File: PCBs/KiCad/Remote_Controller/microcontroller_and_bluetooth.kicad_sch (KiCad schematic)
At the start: 19 parts

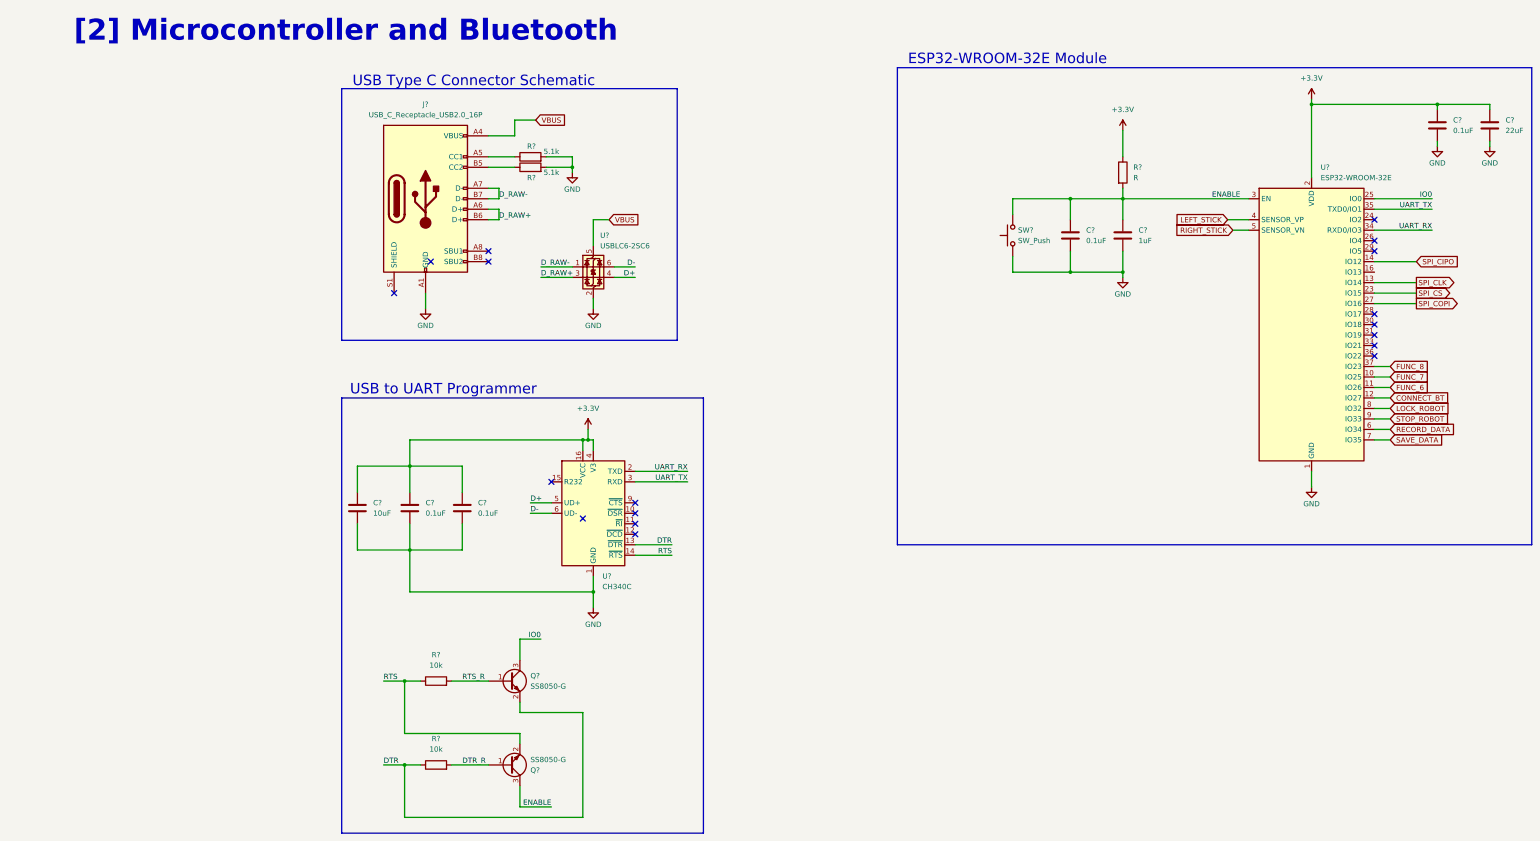
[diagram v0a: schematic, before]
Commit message: Add Power on indicator light, made small corrections
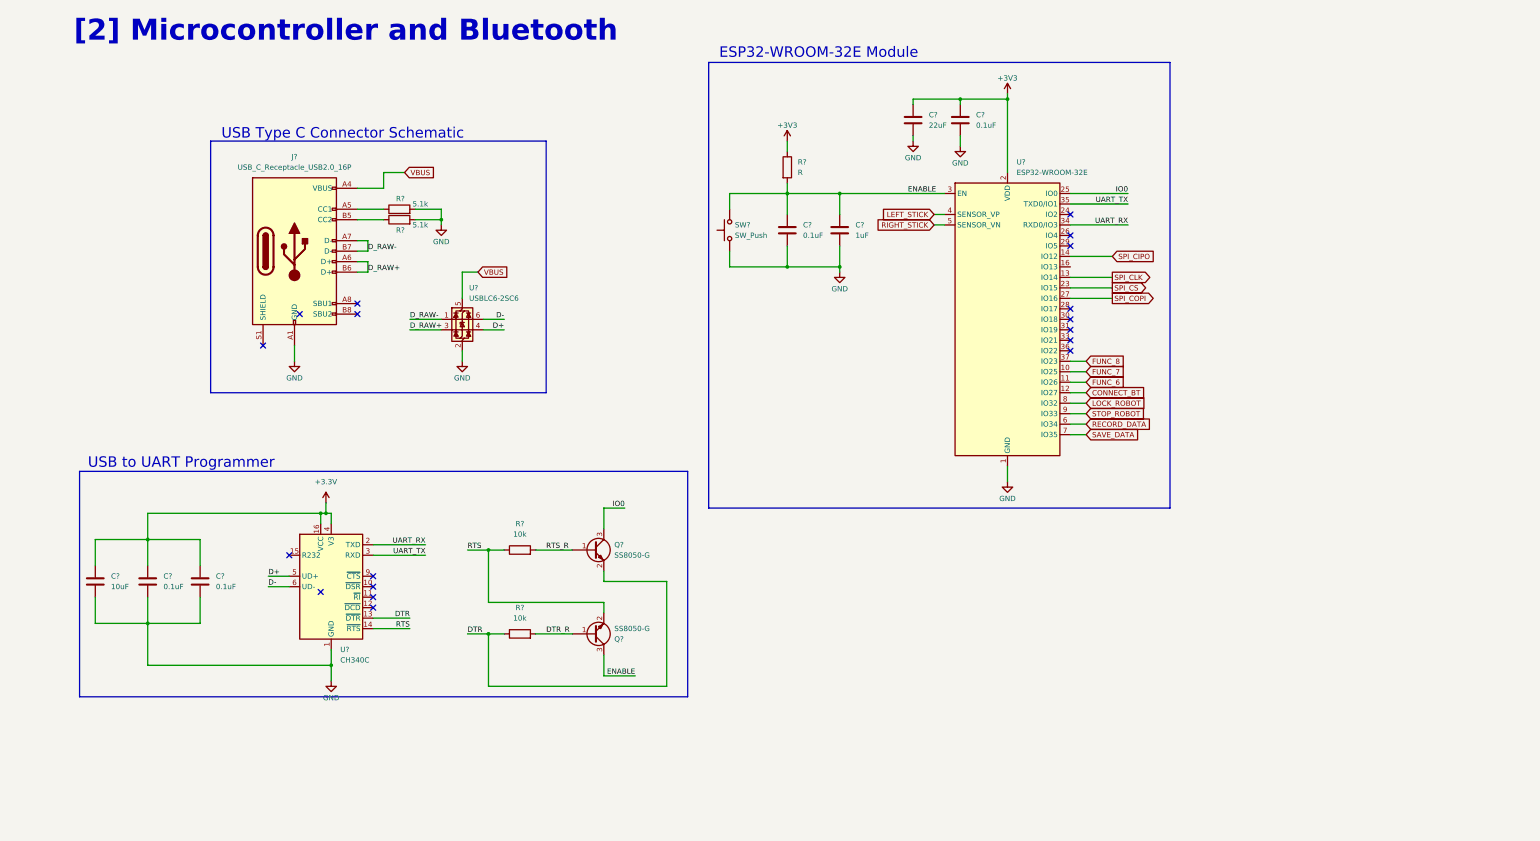
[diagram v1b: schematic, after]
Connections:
- net +3.3V: no longer C?.1, C?.1, R?.1, U?.2 (VDD)
- new net +3V3: C?.1, C?.1, R?.1, U?.2 (VDD)
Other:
- moved on the sheet: C?, J?, Q?, R?, SW?, U?

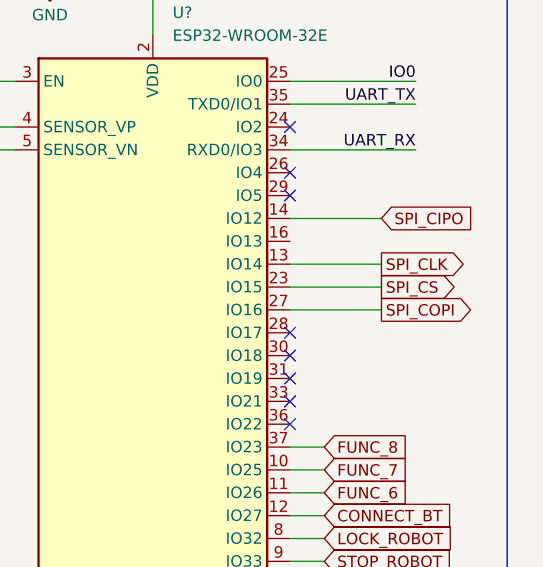
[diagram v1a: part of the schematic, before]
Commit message: Corrected uC-screen connection names
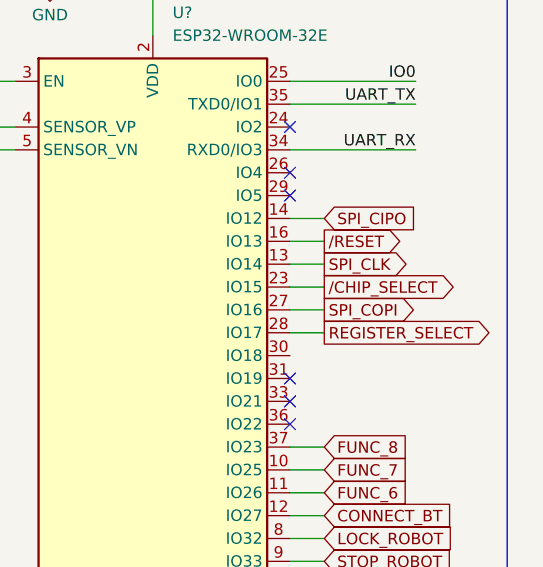
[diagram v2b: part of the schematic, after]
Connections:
- net /RESET: now reaches U?.16 (IO13)
- net REGISTER_SELECT: now reaches U?.28 (IO17)
- net SPI_CS renamed /CHIP_SELECT
- no-connect marks 18 -> 16
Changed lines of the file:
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@@
-	)
-	(no_connect
-		(at 257.81 90.17)
 	)
 	(no_connect
@@
 		(at 88.9 162.56)
 	)
-	(no_connect
-		(at 257.81 92.71)
-	)
 	(wire
 		(pts
@@
 	(wire
 		(pts
-			(xy 257.81 85.09) (xy 267.97 85.09)
+			(xy 261.62 90.17) (xy 257.81 90.17)
+		)
+		(stroke
+			(width 0)
+			(type default)
+		)
+	)
+	(wire
+		(pts
+			(xy 257.81 85.09) (xy 261.62 85.09)
 		)
 		(stroke
@@
 	(wire
 		(pts
+			(xy 261.62 80.01) (xy 257.81 80.01)
+		)
+		(stroke
+			(width 0)
+			(type default)
+		)
+	)
+	(wire
+		(pts
 			(xy 149.86 138.43) (xy 144.78 138.43)
 		)
@@
 	(wire
 		(pts
-			(xy 267.97 82.55) (xy 257.81 82.55)
+			(xy 261.62 82.55) (xy 257.81 82.55)
 		)
 		(stroke
@@
 	(wire
 		(pts
-			(xy 257.81 77.47) (xy 267.97 77.47)
+			(xy 257.81 77.47) (xy 261.62 77.47)
 		)
 		(stroke
@@
 	(wire
 		(pts
-			(xy 267.97 87.63) (xy 257.81 87.63)
+			(xy 261.62 87.63) (xy 257.81 87.63)
 		)
 		(stroke
@@
 			)
 			(justify right bottom)
+		)
+	)
+	(global_label "{slash}RESET"
+		(shape output)
+		(at 261.62 80.01 0)
+		(fields_autoplaced yes)
+		(effects
+			(font
+				(size 1.27 1.27)
+			)
+			(justify left)
+		)
+		(property "Intersheetrefs" "${INTERSHEET_REFS}"
+			(at 271.6808 80.01 0)
+			(effects
+				(font
+					(size 1.27 1.27)
+				)
+				(justify left)
+				(hide yes)
+			)
+		)
+	)
+	(global_label "{slash}CHIP_SELECT"
+		(shape output)
+		(at 261.62 85.09 0)
+		(fields_autoplaced yes)
+		(effects
+			(font
+				(size 1.27 1.27)
+			)
+			(justify left)
+		)
+		(property "Intersheetrefs" "${INTERSHEET_REFS}"
+			(at 278.1518 85.09 0)
+			(effects
+				(font
+					(size 1.27 1.27)
+				)
+				(justify left)
+				(hide yes)
+			)
 		)
 	)
@@
 	(global_label "SPI_CIPO"
 		(shape input)
-		(at 267.97 77.47 0)
+		(at 261.62 77.47 0)
 		(fields_autoplaced yes)
 		(effects
@@
 		)
 		(property "Intersheetrefs" "${INTERSHEET_REFS}"
-			(at 279.4824 77.47 0)
-			(effects
-				(font
-					(size 1.27 1.27)
-				)
-				(justify left)
-				(hide yes)
-			)
-		)
-	)
-	(global_label "SPI_CS"
-		(shape output)
-		(at 267.97 85.09 0)
-		(fields_autoplaced yes)
-		(effects
-			(font
-				(size 1.27 1.27)
-			)
-			(justify left)
-		)
-		(property "Intersheetrefs" "${INTERSHEET_REFS}"
-			(at 277.4866 85.09 0)
+			(at 273.1324 77.47 0)
 			(effects
 				(font
@@
 	(global_label "SPI_CLK"
 		(shape output)
-		(at 267.97 82.55 0)
+		(at 261.62 82.55 0)
 		(fields_autoplaced yes)
 		(effects
@@
 		)
 		(property "Intersheetrefs" "${INTERSHEET_REFS}"
-			(at 278.5752 82.55 0)
+			(at 272.2252 82.55 0)
 			(effects
 				(font
@@
 		)
 	)
+	(global_label "REGISTER_SELECT"
+		(shape output)
+		(at 261.62 90.17 0)
+		(fields_autoplaced yes)
+		(effects
+			(font
+				(size 1.27 1.27)
+			)
+			(justify left)
+		)
+		(property "Intersheetrefs" "${INTERSHEET_REFS}"
+			(at 281.2359 90.17 0)
+			(effects
+				(font
+					(size 1.27 1.27)
+				)
+				(justify left)
+				(hide yes)
+			)
+		)
+	)
 	(global_label "STOP_ROBOT"
 		(shape input)
@@
 	(global_label "SPI_COPI"
 		(shape output)
-		(at 267.97 87.63 0)
+		(at 261.62 87.63 0)
 		(fields_autoplaced yes)
 		(effects
@@
 		)
 		(property "Intersheetrefs" "${INTERSHEET_REFS}"
-			(at 279.4824 87.63 0)
+			(at 273.1324 87.63 0)
 			(effects
 				(font

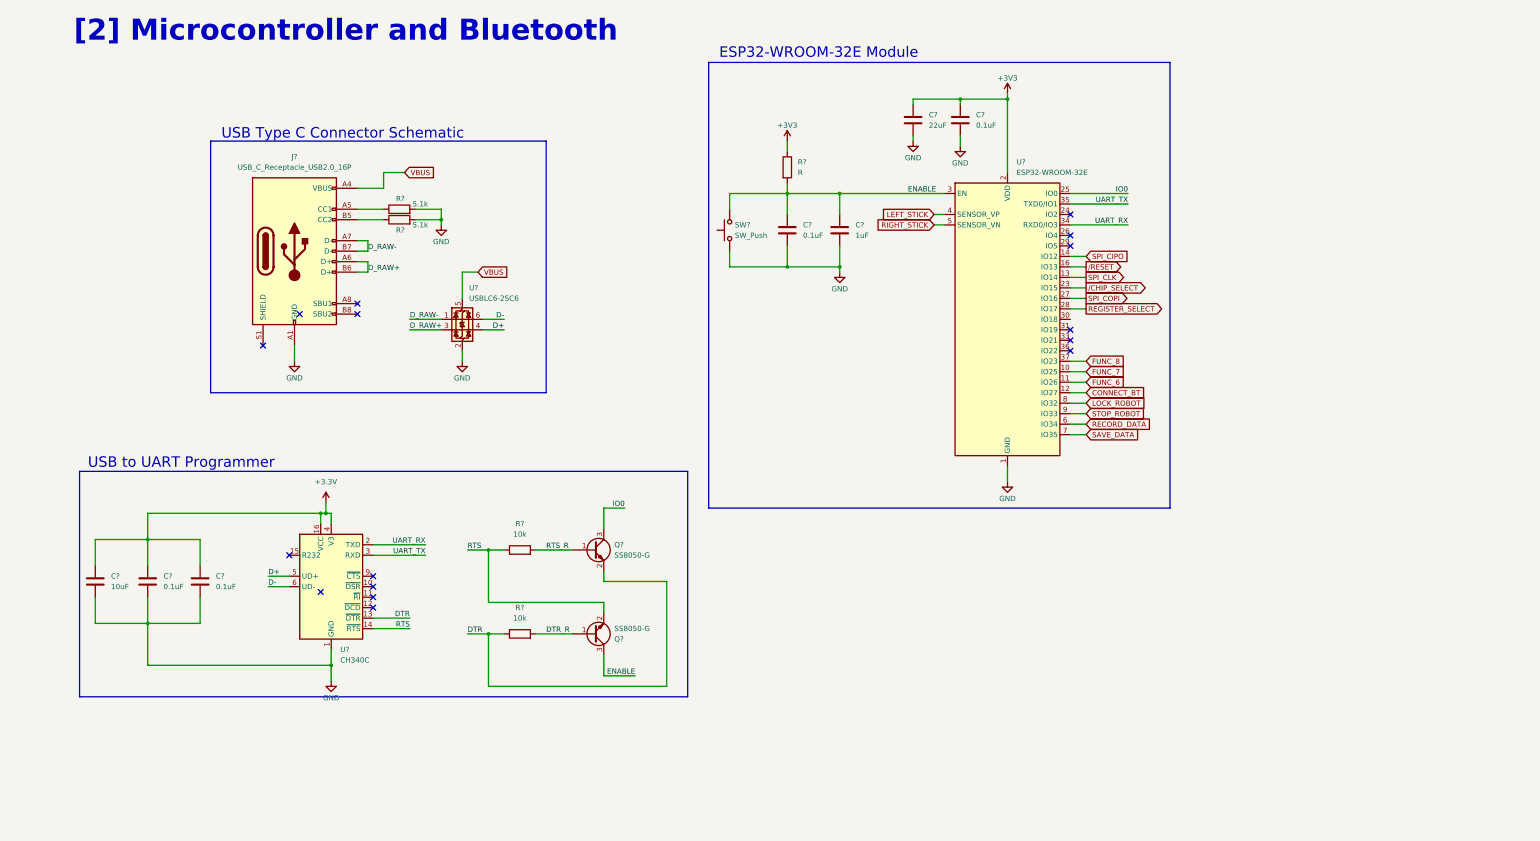
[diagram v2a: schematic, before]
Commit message: Labeled all nets, corrected some labels, added battery-cell symbol
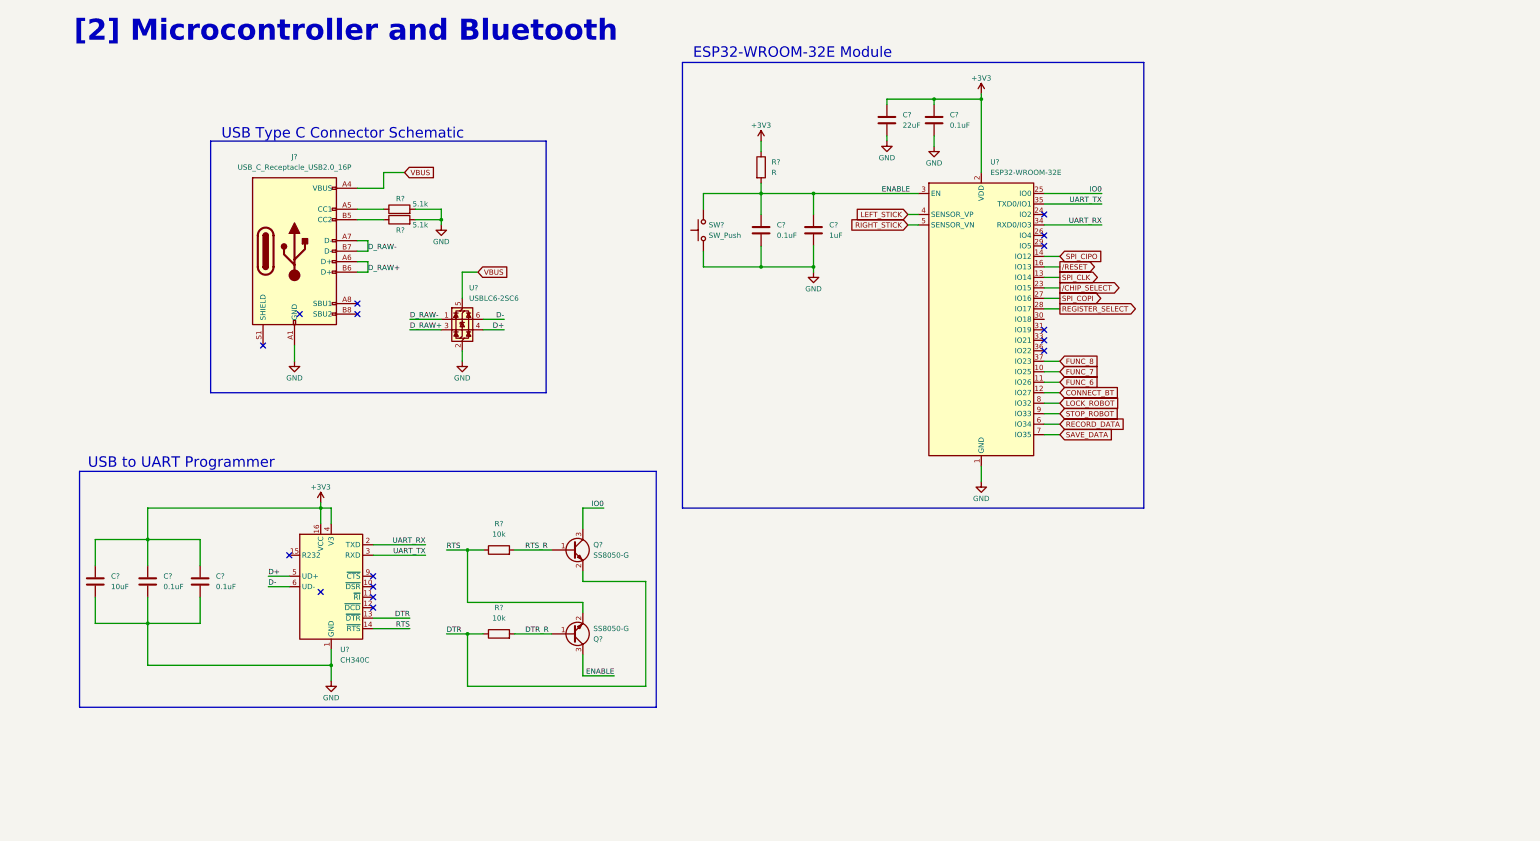
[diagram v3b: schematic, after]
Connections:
- net +3.3V is gone; now on net +3V3: C?.1, C?.1, C?.1, U?.16 (VCC), U?.4 (V3)
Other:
- moved on the sheet: C?, Q?, R?, SW?, U?

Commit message: Annotate components
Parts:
- R201: renamed from R?; value R -> 10k
- gave numbers to parts that had none: 18
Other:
- moved on the sheet: U202

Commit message: Add footprints except connectors, buttons and switches
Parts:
- C201: footprint (none) -> Capacitor_SMD:C_1206_3216Metric
- C202, C203, C204, C206, C207: footprint (none) -> Capacitor_SMD:C_0402_1005Metric
- C205: footprint (none) -> Capacitor_SMD:C_0805_2012Metric
- R201, R204, R205: footprint (none) -> Resistor_SMD:R_0402_1005Metric
- R202, R203: footprint (none) -> Resistor_SMD:R_0603_1608Metric
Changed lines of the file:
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@@
 			)
 		)
-		(property "Footprint" ""
+		(property "Footprint" "Capacitor_SMD:C_0402_1005Metric"
 			(at 225.7552 48.26 0)
 			(effects
@@
 			)
 		)
-		(property "Footprint" ""
+		(property "Footprint" "Capacitor_SMD:C_0805_2012Metric"
 			(at 22.5552 160.02 0)
 			(effects
@@
 			)
 		)
-		(property "Footprint" ""
+		(property "Footprint" "Resistor_SMD:R_0603_1608Metric"
 			(at 95.25 67.818 90)
 			(effects
@@
 			)
 		)
-		(property "Footprint" ""
+		(property "Footprint" "Capacitor_SMD:C_1206_3216Metric"
 			(at 214.3252 48.26 0)
 			(effects
@@
 			)
 		)
-		(property "Footprint" ""
+		(property "Footprint" "Resistor_SMD:R_0603_1608Metric"
 			(at 95.25 70.358 90)
 			(effects
@@
 			)
 		)
-		(property "Footprint" ""
+		(property "Footprint" "Capacitor_SMD:C_0402_1005Metric"
 			(at 47.9552 160.02 0)
 			(effects
@@
 			)
 		)
-		(property "Footprint" ""
+		(property "Footprint" "Resistor_SMD:R_0402_1005Metric"
 			(at 119.38 170.688 90)
 			(effects
@@
 			)
 		)
-		(property "Footprint" ""
+		(property "Footprint" "Capacitor_SMD:C_0402_1005Metric"
 			(at 35.2552 160.02 0)
 			(effects
@@
 			)
 		)
-		(property "Footprint" ""
+		(property "Footprint" "Resistor_SMD:R_0402_1005Metric"
 			(at 181.102 55.88 90)
 			(effects
@@
 			)
 		)
-		(property "Footprint" ""
+		(property "Footprint" "Capacitor_SMD:C_0402_1005Metric"
 			(at 183.8452 74.93 0)
 			(effects
@@
 			)
 		)
-		(property "Footprint" ""
+		(property "Footprint" "Resistor_SMD:R_0402_1005Metric"
 			(at 119.38 150.368 90)
 			(effects
@@
 			)
 		)
-		(property "Footprint" ""
+		(property "Footprint" "Capacitor_SMD:C_0402_1005Metric"
 			(at 196.5452 74.93 0)
 			(effects

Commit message: Add USB receptacle and LCD footprints
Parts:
- J201: footprint (none) -> Connector_USB:USB_C_Receptacle_GCT_USB4105-xx-A_16P_TopMnt_Horizontal
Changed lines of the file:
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@@
 			)
 		)
-		(property "Footprint" ""
+		(property "Footprint" "Connector_USB:USB_C_Receptacle_GCT_USB4105-xx-A_16P_TopMnt_Horizontal"
 			(at 73.66 76.2 0)
 			(effects
